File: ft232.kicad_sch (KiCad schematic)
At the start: 58 parts, among them J1 FT232RL, J12 tp, J13 tp, J14 tp, J15 tp, J16 tp, J17 tp, J18 tp, J19 tp, J2 tp_ft232_, J20 tp, J3 USB_B_Mini, J4 tp_ft232_, J8 tp, Q12 2N7002, Q13 2N7002, Q14 FDN306P, U3 FT232BM, U4 LM1117DT-3.3, U8 93CxxA, Y1 Crystal

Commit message: Add PWR_FLAG symbols to all schematic sheets to fix power_pin_not_driven ERC errors
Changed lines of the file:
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@@
+		)
+	)
+	(symbol
+		(lib_id "power:PWR_FLAG")
+		(at 100.0 50.0 0)
+		(unit 1)
+		(body_style 1)
+		(exclude_from_sim no)
+		(in_bom no)
+		(on_board yes)
+		(in_pos_files no)
+		(dnp no)
+		(property "Reference" "#FLG010"
+			(at 100.0 45.0 0)
+			(hide yes)
+			(show_name no)
+			(do_not_autoplace no)
+			(effects
+				(font
+					(size 1.27 1.27)
+				)
+			)
+		)
+		(property "Value" "PWR_FLAG"
+			(at 100.0 55.0 0)
+			(hide yes)
+			(show_name no)
+			(do_not_autoplace no)
+			(effects
+				(font
+					(size 1.27 1.27)
+				)
+			)
+		)
+		(pin "1"
+			(uuid "b1f1c2d3-e4f5-6789-abcd-ef1234567891-pin1")
+		)
+		(instances
+			(project "esp32_xiaozhi"
+				(path "/cae338e8-f342-43cb-b99a-a0486629133c/62520ce4-d21b-4842-a32d-5b11b343b2aa"
+					(reference "#FLG010")
+					(unit 1)
+				)
+			)
+		)
+	)
+	(symbol
+		(lib_id "power:PWR_FLAG")
+		(at 100.0 100.0 0)
+		(unit 1)
+		(body_style 1)
+		(exclude_from_sim no)
+		(in_bom no)
+		(on_board yes)
+		(in_pos_files no)
+		(dnp no)
+		(property "Reference" "#FLG011"
+			(at 100.0 95.0 0)
+			(hide yes)
+			(show_name no)
+			(do_not_autoplace no)
+			(effects
+				(font
+					(size 1.27 1.27)
+				)
+			)
+		)
+		(property "Value" "PWR_FLAG"
+			(at 100.0 105.0 0)
+			(hide yes)
+			(show_name no)
+			(do_not_autoplace no)
+			(effects
+				(font
+					(size 1.27 1.27)
+				)
+			)
+		)
+		(pin "1"
+			(uuid "b1f1c2d3-e4f5-6789-abcd-ef1234567892-pin1")
+		)
+		(instances
+			(project "esp32_xiaozhi"
+				(path "/cae338e8-f342-43cb-b99a-a0486629133c/62520ce4-d21b-4842-a32d-5b11b343b2aa"
+					(reference "#FLG011")
+					(unit 1)
+				)
+			)
+		)
+	)
+	(symbol
+		(lib_id "power:PWR_FLAG")
+		(at 100.0 150.0 0)
+		(unit 1)
+		(body_style 1)
+		(exclude_from_sim no)
+		(in_bom no)
+		(on_board yes)
+		(in_pos_files no)
+		(dnp no)
+		(property "Reference" "#FLG012"
+			(at 100.0 145.0 0)
+			(hide yes)
+			(show_name no)
+			(do_not_autoplace no)
+			(effects
+				(font
+					(size 1.27 1.27)
+				)
+			)
+		)
+		(property "Value" "PWR_FLAG"
+			(at 100.0 155.0 0)
+			(hide yes)
+			(show_name no)
+			(do_not_autoplace no)
+			(effects
+				(font
+					(size 1.27 1.27)
+				)
+			)
+		)
+		(pin "1"
+			(uuid "b1f1c2d3-e4f5-6789-abcd-ef1234567893-pin1")
+		)
+		(instances
+			(project "esp32_xiaozhi"
+				(path "/cae338e8-f342-43cb-b99a-a0486629133c/62520ce4-d21b-4842-a32d-5b11b343b2aa"
+					(reference "#FLG012")
+					(unit 1)
+				)
+			)
 		)
 	)

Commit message: Revert PWR_FLAG additions - remove '??' squares from schematics
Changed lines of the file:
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@@
-		)
-	)
-	(symbol
-		(lib_id "power:PWR_FLAG")
-		(at 100.0 50.0 0)
-		(unit 1)
-		(body_style 1)
-		(exclude_from_sim no)
-		(in_bom no)
-		(on_board yes)
-		(in_pos_files no)
-		(dnp no)
-		(property "Reference" "#FLG010"
-			(at 100.0 45.0 0)
-			(hide yes)
-			(show_name no)
-			(do_not_autoplace no)
-			(effects
-				(font
-					(size 1.27 1.27)
-				)
-			)
-		)
-		(property "Value" "PWR_FLAG"
-			(at 100.0 55.0 0)
-			(hide yes)
-			(show_name no)
-			(do_not_autoplace no)
-			(effects
-				(font
-					(size 1.27 1.27)
-				)
-			)
-		)
-		(pin "1"
-			(uuid "b1f1c2d3-e4f5-6789-abcd-ef1234567891-pin1")
-		)
-		(instances
-			(project "esp32_xiaozhi"
-				(path "/cae338e8-f342-43cb-b99a-a0486629133c/62520ce4-d21b-4842-a32d-5b11b343b2aa"
-					(reference "#FLG010")
-					(unit 1)
-				)
-			)
-		)
-	)
-	(symbol
-		(lib_id "power:PWR_FLAG")
-		(at 100.0 100.0 0)
-		(unit 1)
-		(body_style 1)
-		(exclude_from_sim no)
-		(in_bom no)
-		(on_board yes)
-		(in_pos_files no)
-		(dnp no)
-		(property "Reference" "#FLG011"
-			(at 100.0 95.0 0)
-			(hide yes)
-			(show_name no)
-			(do_not_autoplace no)
-			(effects
-				(font
-					(size 1.27 1.27)
-				)
-			)
-		)
-		(property "Value" "PWR_FLAG"
-			(at 100.0 105.0 0)
-			(hide yes)
-			(show_name no)
-			(do_not_autoplace no)
-			(effects
-				(font
-					(size 1.27 1.27)
-				)
-			)
-		)
-		(pin "1"
-			(uuid "b1f1c2d3-e4f5-6789-abcd-ef1234567892-pin1")
-		)
-		(instances
-			(project "esp32_xiaozhi"
-				(path "/cae338e8-f342-43cb-b99a-a0486629133c/62520ce4-d21b-4842-a32d-5b11b343b2aa"
-					(reference "#FLG011")
-					(unit 1)
-				)
-			)
-		)
-	)
-	(symbol
-		(lib_id "power:PWR_FLAG")
-		(at 100.0 150.0 0)
-		(unit 1)
-		(body_style 1)
-		(exclude_from_sim no)
-		(in_bom no)
-		(on_board yes)
-		(in_pos_files no)
-		(dnp no)
-		(property "Reference" "#FLG012"
-			(at 100.0 145.0 0)
-			(hide yes)
-			(show_name no)
-			(do_not_autoplace no)
-			(effects
-				(font
-					(size 1.27 1.27)
-				)
-			)
-		)
-		(property "Value" "PWR_FLAG"
-			(at 100.0 155.0 0)
-			(hide yes)
-			(show_name no)
-			(do_not_autoplace no)
-			(effects
-				(font
-					(size 1.27 1.27)
-				)
-			)
-		)
-		(pin "1"
-			(uuid "b1f1c2d3-e4f5-6789-abcd-ef1234567893-pin1")
-		)
-		(instances
-			(project "esp32_xiaozhi"
-				(path "/cae338e8-f342-43cb-b99a-a0486629133c/62520ce4-d21b-4842-a32d-5b11b343b2aa"
-					(reference "#FLG012")
-					(unit 1)
-				)
-			)
 		)
 	)

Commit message: Actualización de esquema y PCB del proyecto ESP32C6 Xiaozhi
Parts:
- J2, J4: footprint Library:connector_pin1 -> TestPoint:TestPoint_THTPad_1.0x1.0mm_Drill0.5mm
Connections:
- net GND1 is gone; now on net GND: C11.2, C12.2, C4.2, C5.2, C6.1, C7.1
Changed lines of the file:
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@@
 	)
 	(junction
-		(at 212.09 96.52)
-		(diameter 0)
-		(color 0 0 0 0)
-	)
-	(junction
 		(at 359.41 49.53)
 		(diameter 0)
@@
 	)
 	(junction
+		(at 212.09 96.52)
+		(diameter 0)
+		(color 0 0 0 0)
+	)
+	(junction
 		(at 204.47 165.1)
 		(diameter 0)
@@
 	(wire
 		(pts
-			(xy 207.01 97.79) (xy 207.01 99.06)
-		)
-		(stroke
-			(width 0)
-			(type default)
-		)
-	)
-	(wire
-		(pts
 			(xy 231.14 200.66) (xy 238.76 200.66)
 		)
@@
 	(wire
 		(pts
+			(xy 212.09 96.52) (xy 212.09 99.06)
+		)
+		(stroke
+			(width 0)
+			(type default)
+		)
+	)
+	(wire
+		(pts
 			(xy 359.41 41.91) (xy 359.41 49.53)
 		)
@@
 	(wire
 		(pts
-			(xy 212.09 96.52) (xy 212.09 99.06)
+			(xy 44.45 157.48) (xy 33.02 157.48)
 		)
 		(stroke
@@
 	(wire
 		(pts
-			(xy 44.45 157.48) (xy 33.02 157.48)
+			(xy 78.74 106.68) (xy 90.17 106.68)
 		)
 		(stroke
@@
 	(wire
 		(pts
-			(xy 78.74 106.68) (xy 90.17 106.68)
+			(xy 306.07 170.18) (xy 298.45 170.18)
 		)
 		(stroke
@@
 	(wire
 		(pts
-			(xy 306.07 170.18) (xy 298.45 170.18)
+			(xy 229.87 129.54) (xy 262.89 129.54)
 		)
 		(stroke
@@
 	(wire
 		(pts
-			(xy 229.87 129.54) (xy 262.89 129.54)
+			(xy 207.01 97.79) (xy 207.01 99.06)
 		)
 		(stroke
@@
 	(wire
 		(pts
-			(xy 233.68 157.48) (xy 233.68 165.1)
+			(xy 97.79 214.63) (xy 101.6 214.63)
 		)
 		(stroke
@@
 	(wire
 		(pts
-			(xy 144.78 96.52) (xy 137.16 96.52)
+			(xy 233.68 157.48) (xy 233.68 165.1)
 		)
 		(stroke
@@
 	(wire
 		(pts
-			(xy 204.47 85.09) (xy 204.47 99.06)
+			(xy 144.78 96.52) (xy 137.16 96.52)
 		)
 		(stroke
@@
 	(wire
 		(pts
-			(xy 266.7 160.02) (xy 266.7 158.75)
+			(xy 204.47 85.09) (xy 204.47 99.06)
 		)
 		(stroke
@@
 	(wire
 		(pts
-			(xy 219.71 208.28) (xy 231.14 208.28)
+			(xy 266.7 160.02) (xy 266.7 158.75)
 		)
 		(stroke
@@
 	(wire
 		(pts
-			(xy 148.59 82.55) (xy 148.59 83.82)
+			(xy 219.71 208.28) (xy 231.14 208.28)
 		)
 		(stroke
@@
 	(wire
 		(pts
-			(xy 97.79 214.63) (xy 101.6 214.63)
+			(xy 148.59 82.55) (xy 148.59 83.82)
 		)
 		(stroke
@@
 			)
 		)
-		(property "Value" "GND1"
-			(at 233.68 99.06 90)
+		(property "Value" "GND"
+			(at 233.68 99.0599 90)
 			(show_name no)
 			(do_not_autoplace no)
@@
 			)
 		)
-		(property "Value" "GND1"
-			(at 254 101.6 0)
+		(property "Value" "GND"
+			(at 256.54 97.7899 0)
 			(show_name no)
 			(do_not_autoplace no)
@@
 					(size 1.27 1.27)
 				)
+				(justify left)
 			)
 		)
@@
 			)
 		)
-		(property "Footprint" "Library:connector_pin1"
+		(property "Footprint" "TestPoint:TestPoint_THTPad_1.0x1.0mm_Drill0.5mm"
 			(at 232.41 93.98 0)
 			(hide yes)
@@
 			)
 		)
-		(property "Value" "GND1"
-			(at 97.79 219.71 0)
+		(property "Value" "GND"
+			(at 100.33 215.8999 0)
 			(show_name no)
 			(do_not_autoplace no)
@@
 					(size 1.27 1.27)
 				)
+				(justify left)
 			)
 		)
@@
 			)
 		)
-		(property "Footprint" "Library:connector_pin1"
+		(property "Footprint" "TestPoint:TestPoint_THTPad_1.0x1.0mm_Drill0.5mm"
 			(at 327.66 43.18 0)
 			(hide yes)

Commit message: Update KiCad schematics/PCB and project files
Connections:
- net DM: now reaches J3.2 (D-), R23.2
- net DP: now reaches J3.3 (D+), R22.2
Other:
- moved on the sheet: J12, J13, J14, J15, J16, J17, J18, J19, J20, J8

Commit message: add files update
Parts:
- added JP17, JP18: jp_xt, Jumper:SolderJumper-2_P1.3mm_Open_RoundedPad1.0x1.5mm, symbol Jumper:Jumper_2_Open
- added Y3: Crystal_GND24_Small_6MHZ, Oscillator:Oscillator_SMD_Abracon_ASE-4Pin_3.2x2.5mm, symbol Device:Crystal_GND24_Small
- R10, R11: value 100 -> 0
- R12, R8: value 10K -> 1k
- R24, U8: now left out of the parts list
- Y1: value Crystal -> 6MHZ Crystal; now left out of the parts list
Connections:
- net FT is gone; now on net MCLR: J17.1 (Pin_1)
- net FT_XTIN: now also JP17.1 (A), Y3.1; no longer Y1.1
- net FT_XTOUT: now also JP18.2 (B), Y3.3; no longer Y1.2
- net GND: now also Y3.2, Y3.4
- new net: JP18.1 (A), Y1.2
- new net: JP17.2 (B), Y1.1
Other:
- moved on the sheet: C15, C16, Y1

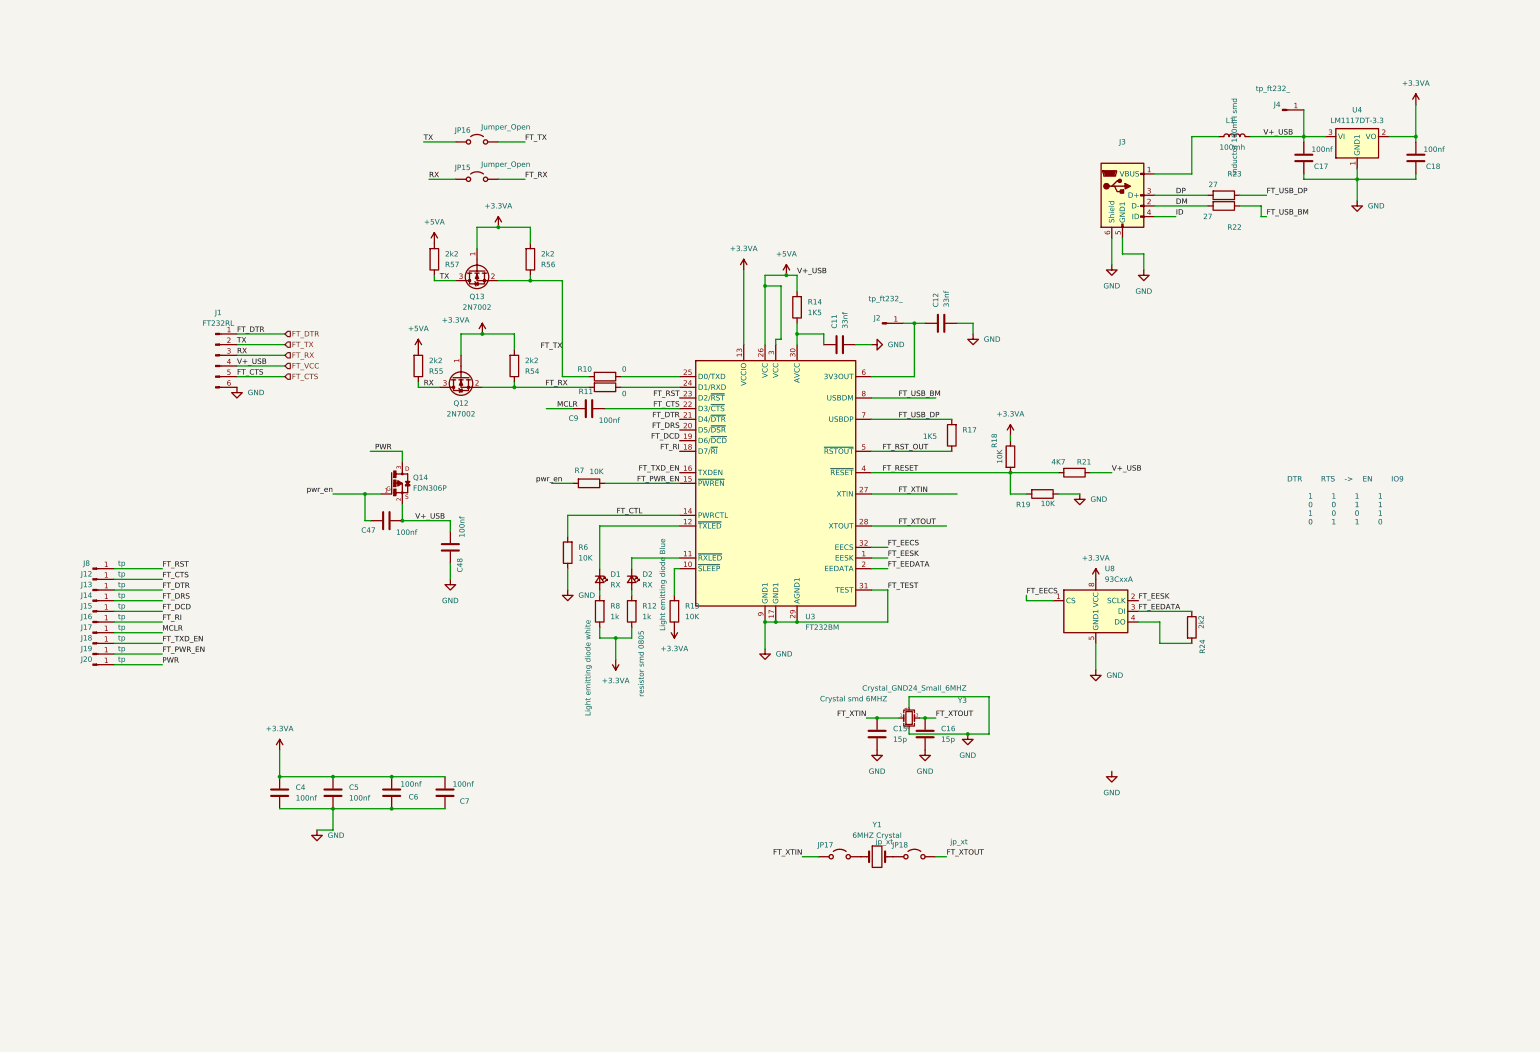
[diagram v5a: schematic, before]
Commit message: Actualización de esquemas y PCB con datos LCSC y librerías JLC
- Añade propiedades LCSC a los símbolos de las hojas de esquema
- Actualiza las hojas TXS0108E, display, esp32_c6, ft232, inmp441,
  led_sw_gpio, max98357a, micro_sd, power_supply y el esquema raíz
- Reorganiza el PCB (footprints, jumpers y nets) y actualiza el proyecto
- Incluye las librerías locales JLCImport (símbolos, huellas y modelos 3D)
  y las entradas correspondientes en fp-lib-table y sym-lib-table
- Añade la documentación técnica en docs/ y el archivo de posiciones
  esp32_xiaozhi-all.pos
- Elimina los ZIP generados gebers.zip y production.zip
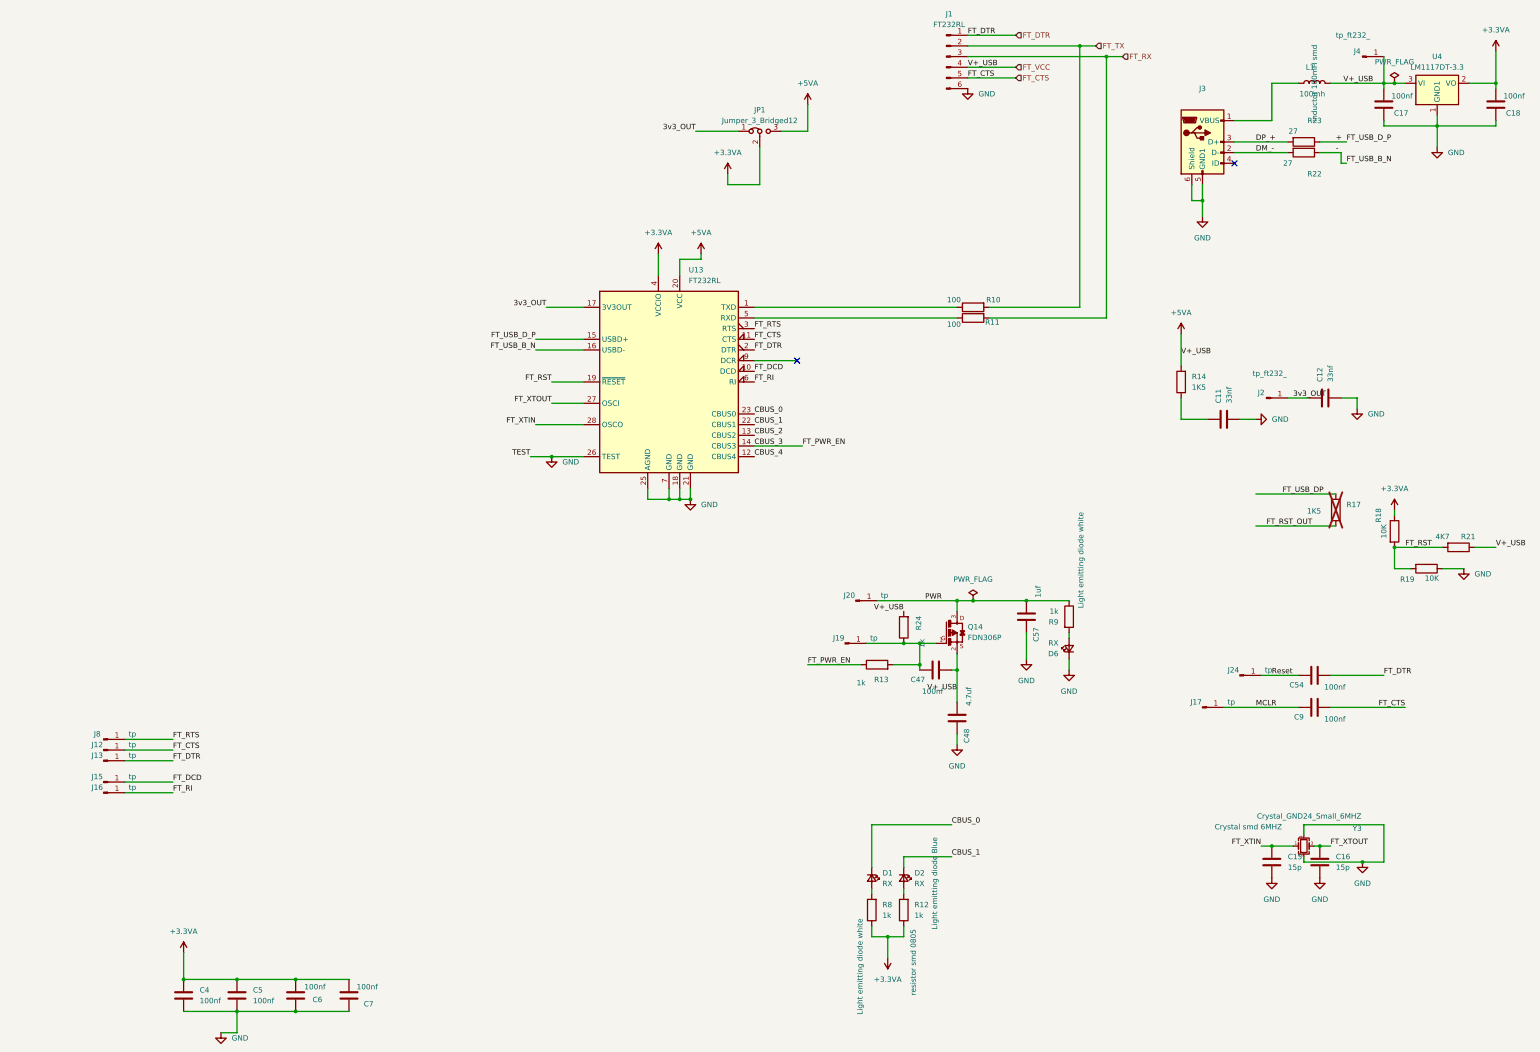
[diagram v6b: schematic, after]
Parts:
- removed J14, J18: tp, TestPoint:TestPoint_Pad_D1.5mm, symbol Connector:Conn_01x01_Pin
- removed JP15, JP16: Jumper_Open, Jumper:SolderJumper-2_P1.3mm_Open_RoundedPad1.0x1.5mm, symbol Jumper:Jumper_2_Open
- removed JP17, JP18: jp_xt, Jumper:SolderJumper-2_P1.3mm_Open_RoundedPad1.0x1.5mm, symbol Jumper:Jumper_2_Open
- removed Q12, Q13: 2N7002, Package_TO_SOT_SMD:SOT-23, symbol Transistor_FET:2N7002
- removed R54, R55, R56, R57: 2k2, Resistor_SMD:R_0805_2012Metric, symbol Device:R
- removed R6: 10K, Resistor_SMD:R_0805_2012Metric, symbol Device:R
- removed R7: 10K, Resistor_SMD:R_0603_1608Metric, symbol Device:R
- removed U3: FT232BM, Package_QFP:LQFP-32_7x7mm_P0.8mm, symbol Interface_USB:FT232BM
- removed U8: 93CxxA, Package_SO:SOIC-8_5.3x5.3mm_P1.27mm, symbol Memory_EEPROM:93CxxA
- removed Y1: 6MHZ Crystal, Crystal:Resonator-2Pin_W10.0mm_H5.0mm, symbol Device:Crystal
- added C54: 100nf, Capacitor_SMD:C_0805_2012Metric, symbol Device:C
- added C57: 1uf, Capacitor_SMD:C_0805_2012Metric, symbol Device:C
- added D6: RX, Diode_SMD:D_0805_2012Metric, symbol Device:LED_Small
- added J24: tp, TestPoint:TestPoint_THTPad_1.0x1.0mm_Drill0.5mm, symbol Connector:Conn_01x01_Pin
- added JP1: Jumper_3_Bridged12, Jumper:SolderJumper-3_P1.3mm_Bridged12_Pad1.0x1.5mm, symbol Jumper:Jumper_3_Bridged12
- added R9: 1k, Resistor_SMD:R_0805_2012Metric, symbol Device:R
- added U13: FT232RL, Package_SO:SSOP-28_5.3x10.2mm_P0.65mm, symbol Interface_USB:FT232RL
- C11, C12: LCSC (none) -> C1739
- C15, C16: LCSC (none) -> C107110
- C17, C18, C4, C47, C5, C6, C7, C9: LCSC (none) -> C1525
- C48: value 100nf -> 4.7uf; LCSC (none) -> C28323
- D1: LCSC (none) -> C2297
- D2: LCSC (none) -> C34499
- J1, J2, J4: now left out of the parts list
- J12, J13, J15, J16, J17, J19, J8: footprint TestPoint:TestPoint_Pad_D1.5mm -> TestPoint:TestPoint_THTPad_1.0x1.0mm_Drill0.5mm; now left out of the parts list
- J20: footprint TestPoint:TestPoint_THTPad_2.0x2.0mm_Drill1.0mm -> TestPoint:TestPoint_THTPad_1.0x1.0mm_Drill0.5mm; now left out of the parts list
- J3: LCSC (none) -> C91144
- L1: LCSC (none) -> C74489
- Q14: LCSC (none) -> C5236682
- R10, R11: value 0 -> 100; LCSC (none) -> C17477
- R12, R8: LCSC (none) -> C17513
- R13: value 10K -> 1k; LCSC (none) -> C17513
- R14: LCSC (none) -> C4310
- R17: LCSC (none) -> C4310; now not fitted; now left out of the parts list
- R18, R19: LCSC (none) -> C17414
- R21: LCSC (none) -> C17673
- R22, R23: LCSC (none) -> C2933393
- R24: value 2k2 -> 1k; LCSC (none) -> C17513; now in the parts list
- U4: LCSC (none) -> C9662
- Y3: LCSC (none) -> C20625731
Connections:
- net FT_EEDATA is gone; now on an unnamed net: R24.1
- net FT_PWR_EN is gone; now on an unnamed net: J19.1 (Pin_1)
- net FT_RESET is gone; now on net FT_RST: R18.2, R19.2, R21.2
- net pwr_en is gone; now on an unnamed net: C47.1, Q14.1
- net +3.3VA: now also JP1.2 (C), U13.4 (VCCIO); no longer R13.1
- net +5VA: now also R24.2, JP1.3 (B), U13.20 (VCC)
- net FT_CTS: now also U13.11 (CTS)
- net FT_DCD: now also U13.10 (DCD)
- net FT_DTR: now also C54.2, U13.2 (DTR)
- net FT_RI: now also U13.6 (RI)
- net FT_RST: now also U13.19 (~{RESET}); no longer J8.1 (Pin_1)
- net FT_USB_DP: no longer R22.1
- net FT_XTIN: now also U13.28 (OSCO)
- net FT_XTOUT: now also U13.27 (OSCI)
- net GND: now also C57.1, D6.1 (K), U13.18 (GND), U13.21 (GND), U13.25 (AGND), U13.26 (TEST), U13.7 (GND)
- net PWR: now also C57.2, R9.1
- net CBUS_1: now reaches D2.1 (K)
- net CBUS_1: now also U13.22 (CBUS1)
- net 3v3_OUT: now reaches C12.1, J2.1 (Pin_1)
- net 3v3_OUT: now also JP1.1 (A), U13.17 (3V3OUT)
- net CBUS_0: now reaches D1.1 (K)
- net CBUS_0: now also U13.23 (CBUS0)
- net at R11.1: now also U13.5 (RXD)
- net at R10.1: now also U13.1 (TXD)
- net DM renamed DM_-
- net DP renamed DP_+
- net FT_USB_BM renamed -
- net -: now also U13.16 (USBD-)
- net ID: no longer names the net of J3.4 (ID)
- new net: D6.2 (A), R9.2
- new net +: R22.1, U13.15 (USBD+)
- new net CBUS_2: U13.13 (CBUS2)
- new net CBUS_3: R13.1, U13.14 (CBUS3)
- new net CBUS_4: U13.12 (CBUS4)
- new net FT_RTS: J8.1 (Pin_1), U13.3 (RTS)
- new net Reset: C54.1, J24.1 (Pin_1)
- no-connect marks 0 -> 2
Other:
- note removed: "DTR RTS -> EN IO9 1 1 1 1 0 0 1 1 1 0 0 1 0 1 1 0"
- moved on the sheet: C11, C12, C15, C16, C17, C18, C4, C47, C48, C5, C6, C7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
